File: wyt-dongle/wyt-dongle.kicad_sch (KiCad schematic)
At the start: 17 parts, among them J1 USB_A, J2 Conn_01x05_Pin, J3 Conn_01x02_Pin, P1 USB_C_Plug_USB2.0, Q1 2N7002, Q2 2N7002, SW1 BOOT, U1 XC6206PxxxMR, U2 ESP32-S2-MINI-2

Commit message: feat: expose more gpios and add reset button
fix: switch to larger LDO

fix: avoid gpio tied to flash for IR LED

fix: connect all usb data pins

fix: add 5.1K resistors for passive usb power
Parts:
- removed U1: XC6206PxxxMR, Package_TO_SOT_SMD:SOT-23-3, symbol Regulator_Linear:XC6206PxxxMR
- added D1: Red LED, LED_SMD:LED_0603_1608Metric, symbol Device:LED
- added D2: Blue LED, LED_SMD:LED_0603_1608Metric, symbol Device:LED
- added J4: Conn_01x08_Pin, Local Library:1x08_Header_Pins_Horizontal, symbol Connector:Conn_01x08_Pin
- added R10, R9: 0R, Resistor_SMD:R_0402_1005Metric, symbol Device:R
- added R11: 10K, Resistor_SMD:R_0402_1005Metric, symbol Device:R
- added R5, R6: 5.1K, Resistor_SMD:R_0402_1005Metric, symbol Device:R
- added R7, R8: 220R, Resistor_SMD:R_0402_1005Metric, symbol Device:R
- added SW1: RESET, Local Library:Xunpu_TS-1088-AR02016, symbol Switch:SW_Push
- added U1: AMS1117-3.3, Package_TO_SOT_SMD:SOT-223-3_TabPin2, symbol Regulator_Linear:AMS1117-3.3
- C1, C2: value 1uF -> 10uF; LCSC C52923 -> C15525
- J1: renamed from J3; now not fitted; now left out of the parts list
- J2: now not fitted; now left out of the parts list
- P1: value USB_C_Plug_USB2.0 -> USB_C_Receptacle_USB2.0_16P; footprint Connector_USB:USB_C_Receptacle_G-Switch_GT-USB-7010ASV -> Connector_USB:USB_C_Receptacle_GCT_USB4105-xx-A_16P_TopMnt_Horizontal; symbol Connector:USB_C_Plug_USB2.0 -> Connector:USB_C_Receptacle_USB2.0_16P; LCSC C2927038 -> C2765186
- R1, R2, R3, R4: footprint Resistor_SMD:R_0603_1608Metric -> Resistor_SMD:R_0402_1005Metric; LCSC C25804 -> C25744
- U2: footprint RF_Module:ESP32-S2-MINI-2 -> PCM_Espressif:ESP32-MINI-1
- renumbered C4 to C3, C3 to C4, J1 to J3, SW1 to SW2
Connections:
- net +3.3V: now also J4.4 (Pin_4), R11.1, R7.2, SW1.2, U1.2 (VO)
- net +5V: now also U1.3 (VI)
- net D+: now also P1.B6 (D+), R10.2, R11.2; no longer U2.24 (IO20)
- net D-: now also P1.B7 (D-), R9.2; no longer U2.23 (IO19)
- net GND: now also D1.1 (K), D2.1 (K), J4.3 (Pin_3), R5.2, R6.1, SW1.1, U1.1 (GND)
- net IR: now also U2.28 (IO33); no longer U2.26 (IO26)
- net SDA: now reaches U2.12 (IO8)
- net SDA: now also J4.2 (Pin_2)
- net SCL: now reaches U2.13 (IO9)
- net SCL: now also J4.1 (Pin_1)
- net CS: now reaches U2.29 (IO34)
- net CS: now also J4.8 (Pin_8)
- net MOSI: now reaches U2.31 (IO35)
- net MOSI: now also J4.7 (Pin_7)
- net SCK: now reaches U2.32 (IO36)
- net SCK: now also J4.6 (Pin_6)
- net MISO: now reaches U2.33 (IO37)
- net MISO: now also J4.5 (Pin_5)
- net at U2.6 (IO2): now also R8.1
- net at P1.A5 (CC1): now also R5.1
- net at P1.B5 (CC2): now also R6.2
- new net: D1.2 (A), R7.1
- new net: D2.2 (A), R8.2
- new net D_N: R9.1, U2.23 (IO19)
- new net D_P: R10.1, U2.24 (IO20)
- no-connect marks 29 -> 24
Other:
- moved on the sheet: C3, SW2

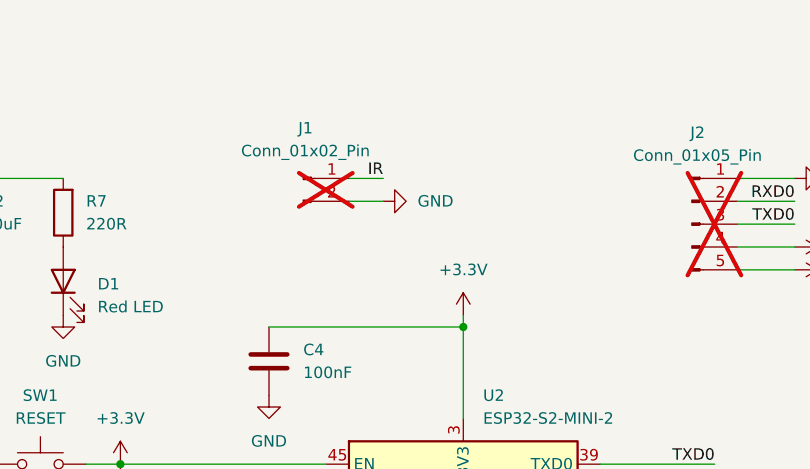
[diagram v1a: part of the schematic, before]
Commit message: chore: space buttons apart for easier flashing
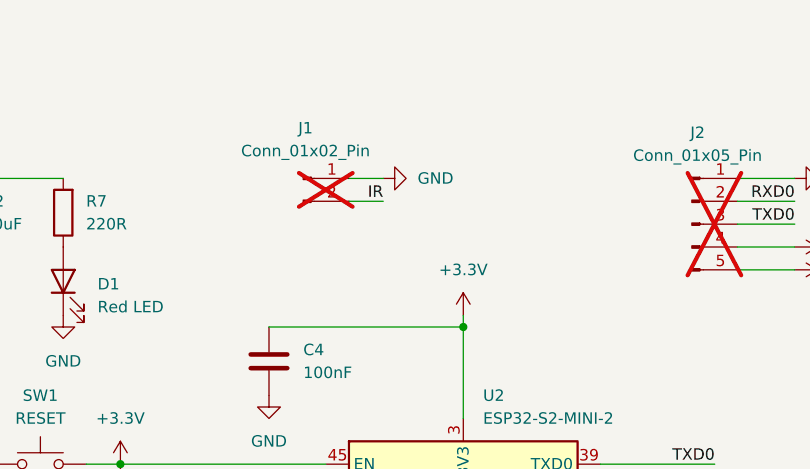
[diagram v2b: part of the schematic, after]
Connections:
- net GND: now also J1.1 (Pin_1); no longer J1.2 (Pin_2)
- net IR: now also J1.2 (Pin_2); no longer J1.1 (Pin_1)
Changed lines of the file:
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@@
 	(wire
 		(pts
-			(xy 151.13 49.53) (xy 147.32 49.53)
+			(xy 151.13 46.99) (xy 147.32 46.99)
 		)
 		(stroke
@@
 	(wire
 		(pts
-			(xy 147.32 46.99) (xy 151.13 46.99)
+			(xy 147.32 49.53) (xy 151.13 49.53)
 		)
 		(stroke
@@
 	)
 	(label "IR"
-		(at 151.13 46.99 180)
+		(at 151.13 49.53 180)
 		(fields_autoplaced yes)
 		(effects
@@
 	(symbol
 		(lib_id "power:GND")
-		(at 151.13 49.53 90)
+		(at 151.13 46.99 90)
 		(unit 1)
 		(exclude_from_sim no)
@@
 		(fields_autoplaced yes)
 		(property "Reference" "#PWR013"
-			(at 157.48 49.53 0)
+			(at 157.48 46.99 0)
 			(effects
 				(font
@@
 		)
 		(property "Value" "GND"
-			(at 154.94 49.5299 90)
+			(at 154.94 46.9899 90)
 			(effects
 				(font
@@
 		)
 		(property "Footprint" ""
-			(at 151.13 49.53 0)
+			(at 151.13 46.99 0)
 			(effects
 				(font
@@
 		)
 		(property "Datasheet" ""
-			(at 151.13 49.53 0)
+			(at 151.13 46.99 0)
 			(effects
 				(font
@@
 		)
 		(property "Description" "Power symbol creates a global label with name \"GND\" , ground"
-			(at 151.13 49.53 0)
-			(effects
-				(font
+			(at 151.13 46.99 0)
+			(effects
+				(font
